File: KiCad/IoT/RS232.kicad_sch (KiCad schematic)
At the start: 14 parts, among them J6 RS232_2, J7 RS232_1, U2 MAX3232, U3 MAX3232

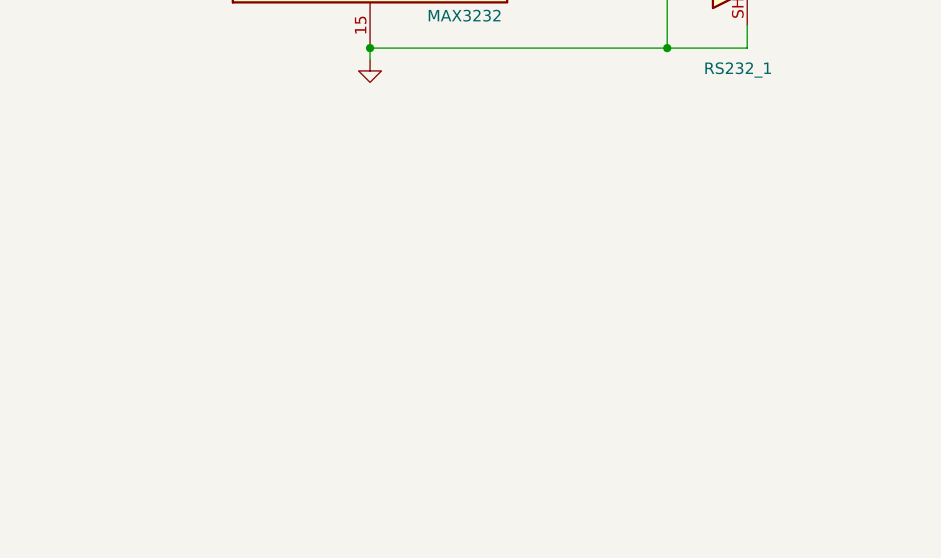
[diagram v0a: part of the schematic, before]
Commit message: updated power schematic
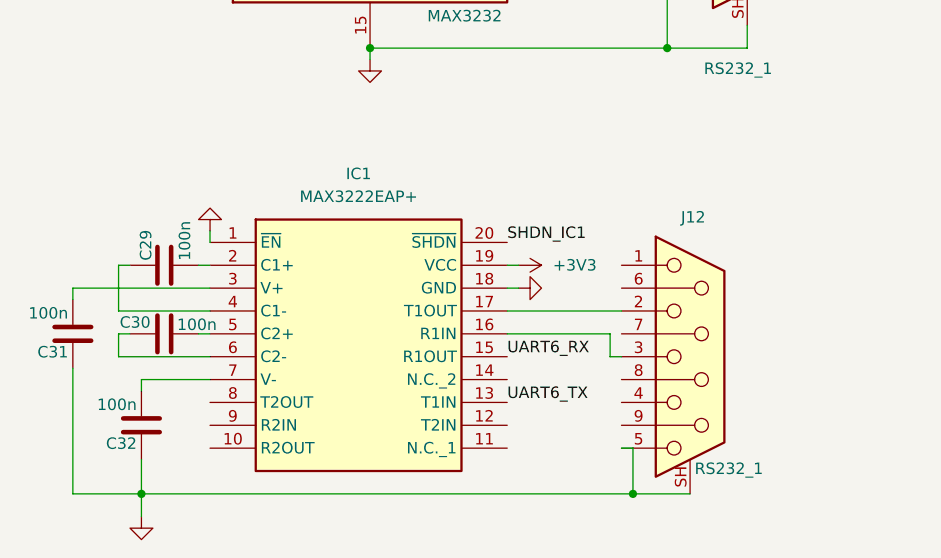
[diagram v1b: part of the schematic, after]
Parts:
- added C29, C30, C31, C32: 100n, symbol Device:C
- added IC1: MAX3222EAP+, Library:SOP65P778X199-20N, symbol New_Library:MAX3222EAP+
- added J12: RS232_1, Connector_Dsub:DSUB-9_Pins_Horizontal_P2.77x2.84mm_EdgePinOffset14.56mm_Housed_MountingHolesOffset15.98mm, symbol Connector:DE9_Socket_MountingHoles
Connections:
- net +3V3: now also IC1.19 (VCC)
- net GND: now also C31.1, C32.1, IC1.1 (~{EN}), IC1.18 (GND), J12.5, J12.SH (PAD)
- net UART6_RX: now also IC1.15 (R1OUT)
- net UART6_TX: now also IC1.13 (T1IN)
- new net: C32.2, IC1.7 (V-)
- new net: C31.2, IC1.3 (V+)
- new net: IC1.16 (R1IN), J12.3
- new net: IC1.17 (T1OUT), J12.2
- new net: C29.2, IC1.2 (C1+)
- new net: C29.1, IC1.4 (C1-)
- new net: C30.2, IC1.5 (C2+)
- new net: C30.1, IC1.6 (C2-)
- new net SHDN_IC1: IC1.20 (~{SHDN})

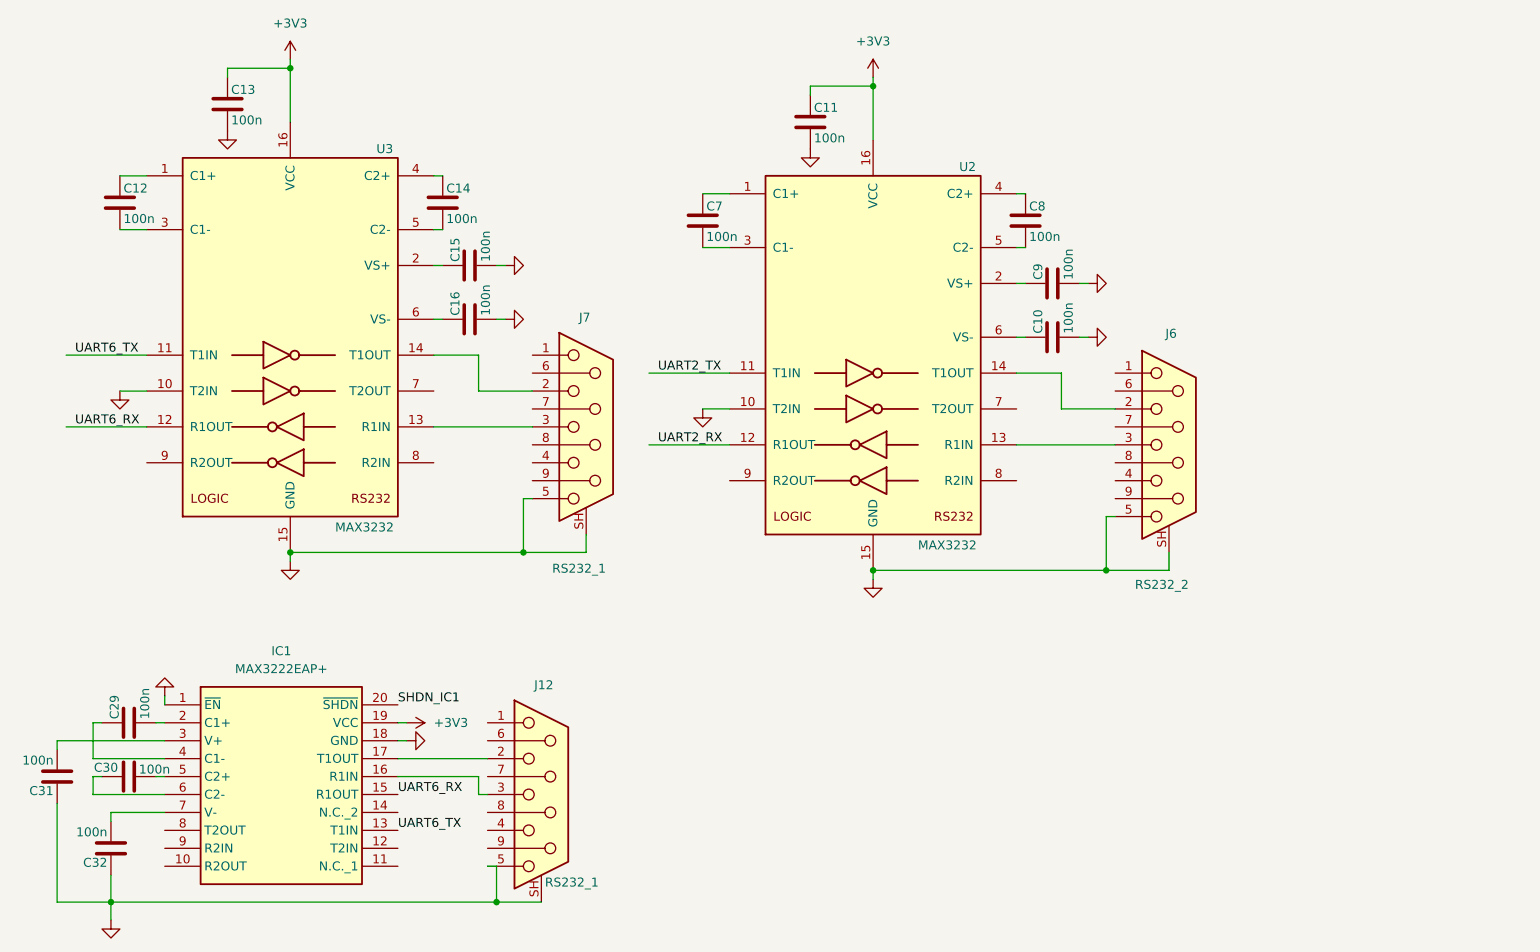
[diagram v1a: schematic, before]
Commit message: added buttons, connected leds, changed uart ic and added crystals
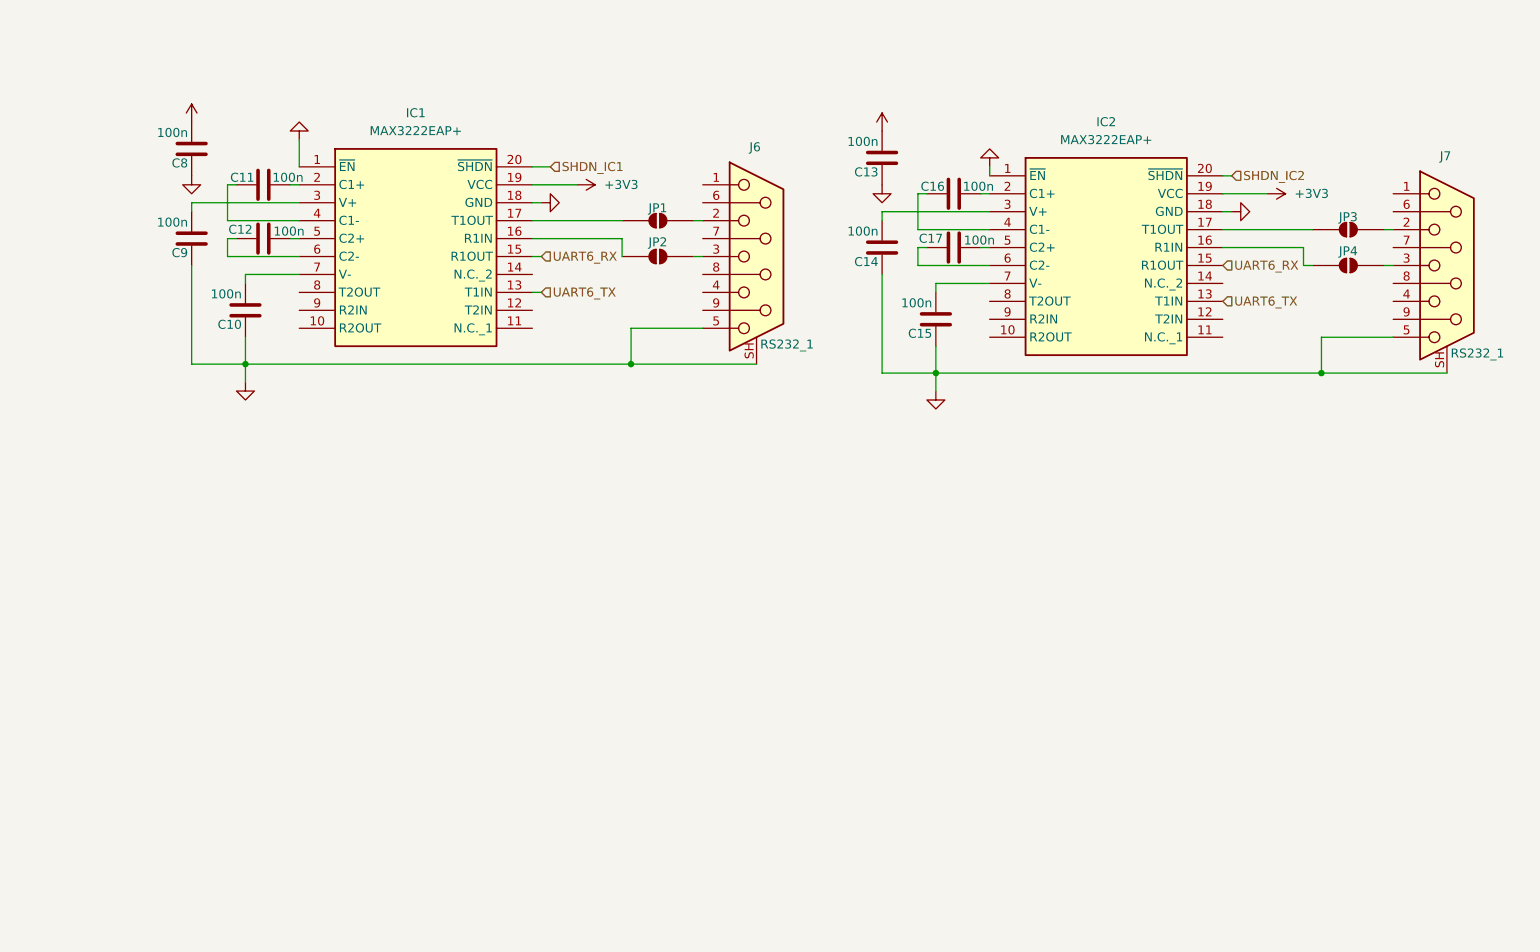
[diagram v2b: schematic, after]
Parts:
- removed C10, C11, C12, C7, C9: 100n, symbol Device:C
- removed J6: RS232_2, Connector_Dsub:DSUB-9_Pins_Horizontal_P2.77x2.84mm_EdgePinOffset14.56mm_Housed_MountingHolesOffset15.98mm, symbol Connector:DE9_Socket_MountingHoles
- removed U2, U3: MAX3232, symbol Interface_UART:MAX3232
- added C17: 100n, Capacitor_SMD:C_0603_1608Metric_Pad1.08x0.95mm_HandSolder, symbol Device:C
- added IC2: MAX3222EAP+, Library:SOP65P778X199-20N, symbol New_Library:MAX3222EAP+
- added JP1, JP2, JP3, JP4: SolderJumper_2_Open, Package_SON:WSON-8-1EP_6x5mm_P1.27mm_EP3.4x4mm, symbol Jumper:SolderJumper_2_Open
- C10: renamed from C32; footprint (none) -> Capacitor_SMD:C_0603_1608Metric_Pad1.08x0.95mm_HandSolder
- C11: renamed from C29; footprint (none) -> Capacitor_SMD:C_0603_1608Metric_Pad1.08x0.95mm_HandSolder
- C12: renamed from C30; footprint (none) -> Capacitor_SMD:C_0603_1608Metric_Pad1.08x0.95mm_HandSolder
- C13, C14, C15, C16, C8: footprint (none) -> Capacitor_SMD:C_0603_1608Metric_Pad1.08x0.95mm_HandSolder
- C9: renamed from C31; footprint (none) -> Capacitor_SMD:C_0603_1608Metric_Pad1.08x0.95mm_HandSolder
- renumbered J12 to J6
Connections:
- net +3V3: now also C13.2, C8.2, IC2.19 (VCC); no longer C13.1
- net GND: now also C13.1, C14.1, C15.1, C8.1, IC2.1 (~{EN}), IC2.18 (GND); no longer C13.2, C15.2, C16.2
- net UART6_RX: now also IC2.15 (R1OUT)
- net UART6_TX: now also IC2.13 (T1IN)
- net at IC1.16 (R1IN): now also JP2.1 (A); no longer J6.3
- net at IC1.17 (T1OUT): now also JP1.1 (A); no longer J6.2
- net at C16.1: now also IC2.4 (C1-)
- net at J7.3: now also JP4.2 (B)
- net at J7.2: now also JP3.2 (B)
- net at C14.2: now also IC2.3 (V+)
- new net: C16.2, IC2.2 (C1+)
- new net: C17.1, IC2.6 (C2-)
- new net: C17.2, IC2.5 (C2+)
- new net: J6.3, JP2.2 (B)
- new net: IC2.16 (R1IN), JP4.1 (A)
- new net: IC2.17 (T1OUT), JP3.1 (A)
- new net: C15.2, IC2.7 (V-)
- new net: J6.2, JP1.2 (B)
- new net SHDN_IC2: IC2.20 (~{SHDN})
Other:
- moved on the sheet: C10, C11, C12, C9, IC1, J6

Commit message: minor fixes and cleanup
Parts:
- renumbered C8 to C13, C9 to C14, C10 to C15, C11 to C16, C12 to C17, C13 to C18, C14 to C19, C15 to C20, C16 to C21, C17 to C22, J6 to J7, J7 to J8, JP1 to JP5, JP2 to JP6, JP3 to JP7, JP4 to JP8
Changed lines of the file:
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@@
 		(in_pos_files yes)
 		(dnp no)
-		(property "Reference" "C16"
+		(property "Reference" "C21"
 			(at 147.32 39.624 90)
 			(show_name no)
@@
 			(project "IoT"
 				(path "/f5d15b22-d91e-4545-b7af-da23c1769042/43c31ab3-a50b-4c6f-a99c-c41c2f249985"
-					(reference "C16")
+					(reference "C21")
 					(unit 1)
 				)
@@
 		(dnp no)
 		(fields_autoplaced yes)
-		(property "Reference" "#PWR024"
+		(property "Reference" "#PWR036"
 			(at 91.44 39.37 0)
 			(hide yes)
@@
 			(project "IoT"
 				(path "/f5d15b22-d91e-4545-b7af-da23c1769042/43c31ab3-a50b-4c6f-a99c-c41c2f249985"
-					(reference "#PWR024")
+					(reference "#PWR036")
 					(unit 1)
 				)
@@
 		(dnp no)
 		(fields_autoplaced yes)
-		(property "Reference" "#PWR023"
+		(property "Reference" "#PWR035"
 			(at 96.52 41.91 0)
 			(hide yes)
@@
 			(project "IoT"
 				(path "/f5d15b22-d91e-4545-b7af-da23c1769042/43c31ab3-a50b-4c6f-a99c-c41c2f249985"
-					(reference "#PWR023")
+					(reference "#PWR035")
 					(unit 1)
 				)
@@
 		(dnp no)
 		(fields_autoplaced yes)
-		(property "Reference" "#PWR025"
+		(property "Reference" "#PWR037"
 			(at 138.43 35.56 0)
 			(hide yes)
@@
 			(project "IoT"
 				(path "/f5d15b22-d91e-4545-b7af-da23c1769042/43c31ab3-a50b-4c6f-a99c-c41c2f249985"
-					(reference "#PWR025")
+					(reference "#PWR037")
 					(unit 1)
 				)
@@
 		(dnp no)
 		(fields_autoplaced yes)
-		(property "Reference" "#PWR022"
+		(property "Reference" "#PWR034"
 			(at 55.88 26.67 0)
 			(hide yes)
@@
 			(project "IoT"
 				(path "/f5d15b22-d91e-4545-b7af-da23c1769042/43c31ab3-a50b-4c6f-a99c-c41c2f249985"
-					(reference "#PWR022")
+					(reference "#PWR034")
 					(unit 1)
 				)
@@
 		(dnp no)
 		(fields_autoplaced yes)
-		(property "Reference" "#PWR026"
+		(property "Reference" "#PWR038"
 			(at 138.43 45.72 0)
 			(hide yes)
@@
 			(project "IoT"
 				(path "/f5d15b22-d91e-4545-b7af-da23c1769042/43c31ab3-a50b-4c6f-a99c-c41c2f249985"
-					(reference "#PWR026")
+					(reference "#PWR038")
 					(unit 1)
 				)
@@
 		(in_pos_files yes)
 		(dnp no)
-		(property "Reference" "C17"
+		(property "Reference" "C22"
 			(at 147.066 46.99 90)
 			(show_name no)
@@
 			(project "IoT"
 				(path "/f5d15b22-d91e-4545-b7af-da23c1769042/43c31ab3-a50b-4c6f-a99c-c41c2f249985"
-					(reference "C17")
+					(reference "C22")
 					(unit 1)
 				)
@@
 		(dnp no)
 		(fields_autoplaced yes)
-		(property "Reference" "#PWR027"
+		(property "Reference" "#PWR039"
 			(at 146.05 74.93 0)
 			(hide yes)
@@
 			(project "IoT"
 				(path "/f5d15b22-d91e-4545-b7af-da23c1769042/43c31ab3-a50b-4c6f-a99c-c41c2f249985"
-					(reference "#PWR027")
+					(reference "#PWR039")
 					(unit 1)
 				)
@@
 		(in_pos_files yes)
 		(dnp no)
-		(property "Reference" "C8"
+		(property "Reference" "C13"
 			(at 40.132 36.322 0)
 			(show_name no)
@@
 			(project "IoT"
 				(path "/f5d15b22-d91e-4545-b7af-da23c1769042/43c31ab3-a50b-4c6f-a99c-c41c2f249985"
-					(reference "C8")
+					(reference "C13")
 					(unit 1)
 				)
@@
 		(in_pos_files yes)
 		(dnp no)
-		(property "Reference" "C10"
+		(property "Reference" "C15"
 			(at 47.752 59.182 0)
 			(show_name no)
@@
 			(project "IoT"
 				(path "/f5d15b22-d91e-4545-b7af-da23c1769042/43c31ab3-a50b-4c6f-a99c-c41c2f249985"
-					(reference "C10")
+					(reference "C15")
 					(unit 1)
 				)
@@
 		(in_pos_files yes)
 		(dnp no)
-		(property "Reference" "JP2"
+		(property "Reference" "JP6"
 			(at 106.68 47.498 0)
 			(show_name no)
@@
 			(project "IoT"
 				(path "/f5d15b22-d91e-4545-b7af-da23c1769042/43c31ab3-a50b-4c6f-a99c-c41c2f249985"
-					(reference "JP2")
+					(reference "JP6")
 					(unit 1)
 				)
@@
 		(in_pos_files yes)
 		(dnp no)
-		(property "Reference" "C14"
+		(property "Reference" "C19"
 			(at 137.922 50.292 0)
 			(show_name no)
@@
 			(project "IoT"
 				(path "/f5d15b22-d91e-4545-b7af-da23c1769042/43c31ab3-a50b-4c6f-a99c-c41c2f249985"
-					(reference "C14")
+					(reference "C19")
 					(unit 1)
 				)
@@
 		(in_pos_files yes)
 		(dnp no)
-		(property "Reference" "C9"
+		(property "Reference" "C14"
 			(at 40.132 49.022 0)
 			(show_name no)
@@
 			(project "IoT"
 				(path "/f5d15b22-d91e-4545-b7af-da23c1769042/43c31ab3-a50b-4c6f-a99c-c41c2f249985"
-					(reference "C9")
+					(reference "C14")
 					(unit 1)
 				)
@@
 		(in_pos_files yes)
 		(dnp no)
-		(property "Reference" "C15"
+		(property "Reference" "C20"
 			(at 145.542 60.452 0)
 			(show_name no)
@@
 			(project "IoT"
 				(path "/f5d15b22-d91e-4545-b7af-da23c1769042/43c31ab3-a50b-4c6f-a99c-c41c2f249985"
-					(reference "C15")
+					(reference "C20")
 					(unit 1)
 				)
@@
 		(in_pos_files yes)
 		(dnp no)
-		(property "Reference" "J7"
+		(property "Reference" "J8"
 			(at 217.424 35.306 0)
 			(show_name no)
@@
 			(project "IoT"
 				(path "/f5d15b22-d91e-4545-b7af-da23c1769042/43c31ab3-a50b-4c6f-a99c-c41c2f249985"
-					(reference "J7")
+					(reference "J8")
 					(unit 1)
 				)
@@
 		(in_pos_files yes)
 		(dnp no)
-		(property "Reference" "C13"
+		(property "Reference" "C18"
 			(at 137.922 37.592 0)
 			(show_name no)
@@
 			(project "IoT"
 				(path "/f5d15b22-d91e-4545-b7af-da23c1769042/43c31ab3-a50b-4c6f-a99c-c41c2f249985"
-					(reference "C13")
+					(reference "C18")
 					(unit 1)
 				)
@@
 		(in_pos_files yes)
 		(dnp no)
-		(property "Reference" "J6"
+		(property "Reference" "J7"
 			(at 119.634 34.036 0)
 			(show_name no)
@@
 			(project "IoT"
 				(path "/f5d15b22-d91e-4545-b7af-da23c1769042/43c31ab3-a50b-4c6f-a99c-c41c2f249985"
-					(reference "J6")
+					(reference "J7")
 					(unit 1)
 				)
@@
 		(in_pos_files yes)
 		(dnp no)
-		(property "Reference" "JP1"
+		(property "Reference" "JP5"
 			(at 106.68 42.672 0)
 			(show_name no)
@@
 			(project "IoT"
 				(path "/f5d15b22-d91e-4545-b7af-da23c1769042/43c31ab3-a50b-4c6f-a99c-c41c2f249985"
-					(reference "JP1")
+					(reference "JP5")
 					(unit 1)
 				)
@@
 		(dnp no)
 		(fields_autoplaced yes)
-		(property "Reference" "#PWR029"
+		(property "Reference" "#PWR041"
 			(at 194.31 43.18 0)
 			(hide yes)
@@
 			(project "IoT"
 				(path "/f5d15b22-d91e-4545-b7af-da23c1769042/43c31ab3-a50b-4c6f-a99c-c41c2f249985"
-					(reference "#PWR029")
+					(reference "#PWR041")
 					(unit 1)
 				)
@@
 		(in_pos_files yes)
 		(dnp no)
-		(property "Reference" "JP4"
+		(property "Reference" "JP8"
 			(at 204.47 48.768 0)
 			(show_name no)
@@
 			(project "IoT"
 				(path "/f5d15b22-d91e-4545-b7af-da23c1769042/43c31ab3-a50b-4c6f-a99c-c41c2f249985"
-					(reference "JP4")
+					(reference "JP8")
 					(unit 1)
 				)
@@
 		(dnp no)
 		(fields_autoplaced yes)
-		(property "Reference" "#PWR021"
+		(property "Reference" "#PWR033"
 			(at 48.26 73.66 0)
 			(hide yes)
@@
 			(project "IoT"
 				(path "/f5d15b22-d91e-4545-b7af-da23c1769042/43c31ab3-a50b-4c6f-a99c-c41c2f249985"
-					(reference "#PWR021")
+					(reference "#PWR033")
 					(unit 1)
 				)
@@
 		(dnp no)
 		(fields_autoplaced yes)
-		(property "Reference" "#PWR030"
+		(property "Reference" "#PWR042"
 			(at 189.23 40.64 0)
 			(hide yes)
@@
 			(project "IoT"
 				(path "/f5d15b22-d91e-4545-b7af-da23c1769042/43c31ab3-a50b-4c6f-a99c-c41c2f249985"
-					(reference "#PWR030")
+					(reference "#PWR042")
 					(unit 1)
 				)
@@
 		(dnp no)
 		(fields_autoplaced yes)
-		(property "Reference" "#PWR019"
+		(property "Reference" "#PWR031"
 			(at 40.64 34.29 0)
 			(hide yes)
@@
 			(project "IoT"
 				(path "/f5d15b22-d91e-4545-b7af-da23c1769042/43c31ab3-a50b-4c6f-a99c-c41c2f249985"
-					(reference "#PWR019")
+					(reference "#PWR031")
 					(unit 1)
 				)
@@
 		(in_pos_files yes)
 		(dnp no)
-		(property "Reference" "JP3"
+		(property "Reference" "JP7"
 			(at 204.47 43.942 0)
 			(show_name no)
@@
 			(project "IoT"
 				(path "/f5d15b22-d91e-4545-b7af-da23c1769042/43c31ab3-a50b-4c6f-a99c-c41c2f249985"
-					(reference "JP3")
+					(reference "JP7")
 					(unit 1)
 				)
@@
 		(in_pos_files yes)
 		(dnp no)
-		(property "Reference" "C11"
+		(property "Reference" "C16"
 			(at 49.53 38.354 90)
 			(show_name no)
@@
 			(project "IoT"
 				(path "/f5d15b22-d91e-4545-b7af-da23c1769042/43c31ab3-a50b-4c6f-a99c-c41c2f249985"
-					(reference "C11")
+					(reference "C16")
 					(unit 1)
 				)
@@
 		(dnp no)
 		(fields_autoplaced yes)
-		(property "Reference" "#PWR028"
+		(property "Reference" "#PWR040"
 			(at 153.67 30.48 0)
 			(hide yes)
@@
 			(project "IoT"
 				(path "/f5d15b22-d91e-4545-b7af-da23c1769042/43c31ab3-a50b-4c6f-a99c-c41c2f249985"
-					(reference "#PWR028")
+					(reference "#PWR040")
 					(unit 1)
 				)
@@
 		(in_pos_files yes)
 		(dnp no)
-		(property "Reference" "C12"
+		(property "Reference" "C17"
 			(at 49.276 45.72 90)
 			(show_name no)
@@
 			(project "IoT"
 				(path "/f5d15b22-d91e-4545-b7af-da23c1769042/43c31ab3-a50b-4c6f-a99c-c41c2f249985"
-					(reference "C12")
+					(reference "C17")
 					(unit 1)
 				)
@@
 		(dnp no)
 		(fields_autoplaced yes)
-		(property "Reference" "#PWR020"
+		(property "Reference" "#PWR032"
 			(at 40.64 44.45 0)
 			(hide yes)
@@
 			(project "IoT"
 				(path "/f5d15b22-d91e-4545-b7af-da23c1769042/43c31ab3-a50b-4c6f-a99c-c41c2f249985"
-					(reference "#PWR020")
-					(unit 1)
-				)
+					(reference "#PWR032")
+					(unit 1)
+				)
